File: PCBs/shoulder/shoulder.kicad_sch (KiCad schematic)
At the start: 4 parts

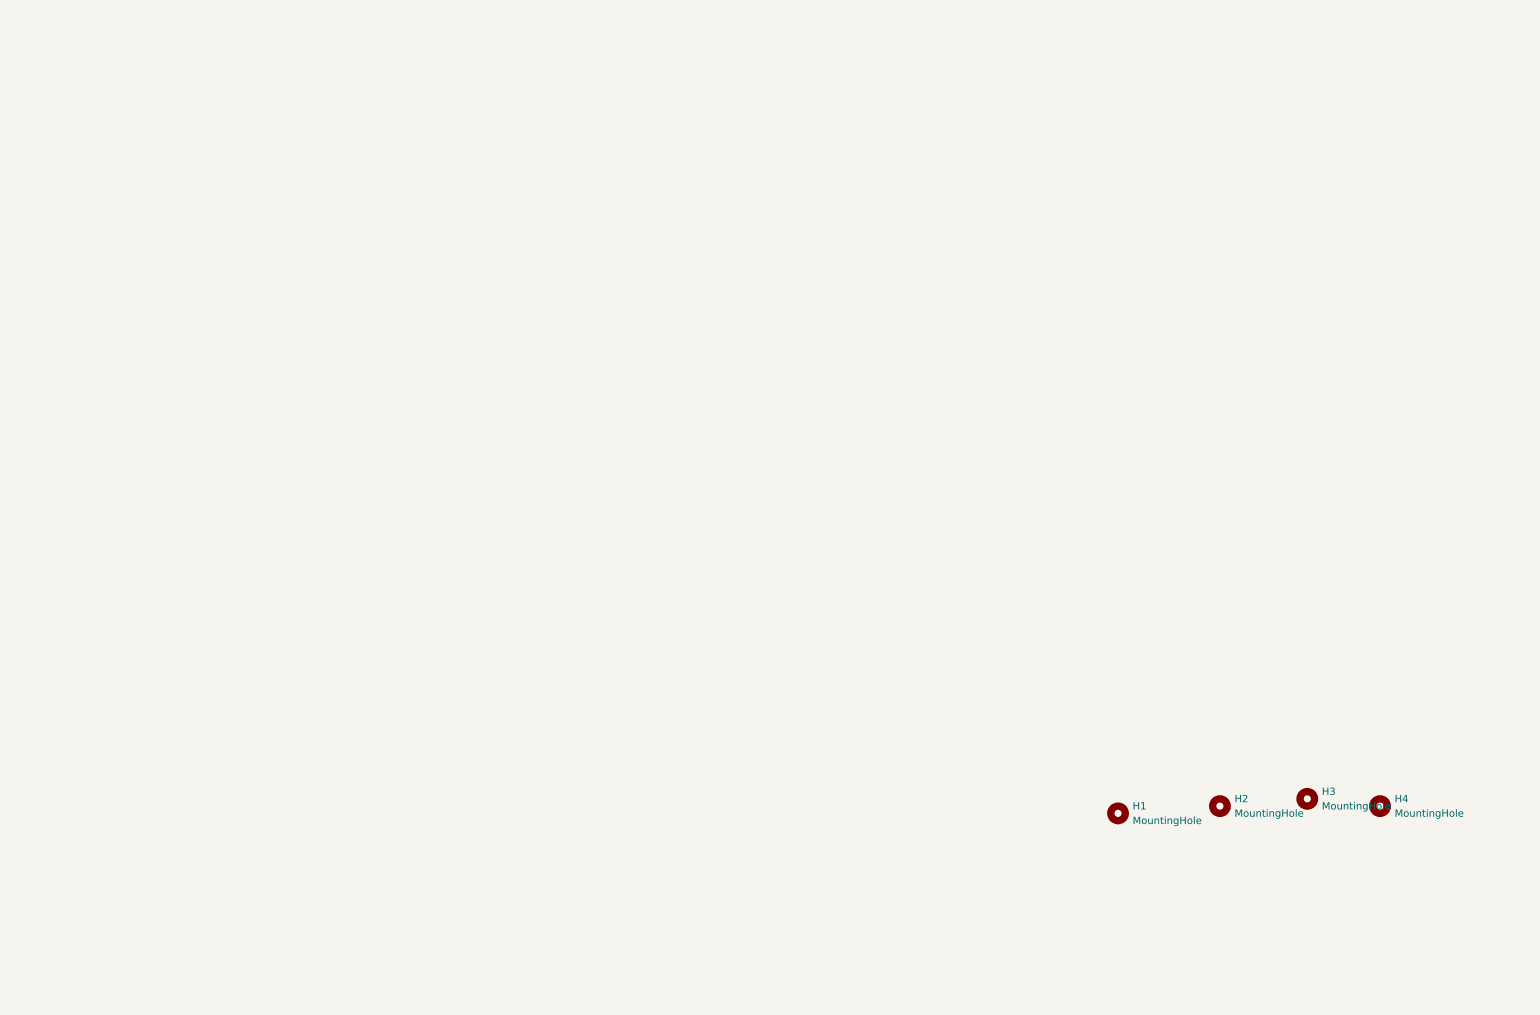
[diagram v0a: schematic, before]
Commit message: Shoulder motor assy almost done. Need to find a library for the 2N551 NPN and redo the circuit. Ensure that the footprint pinout is correct
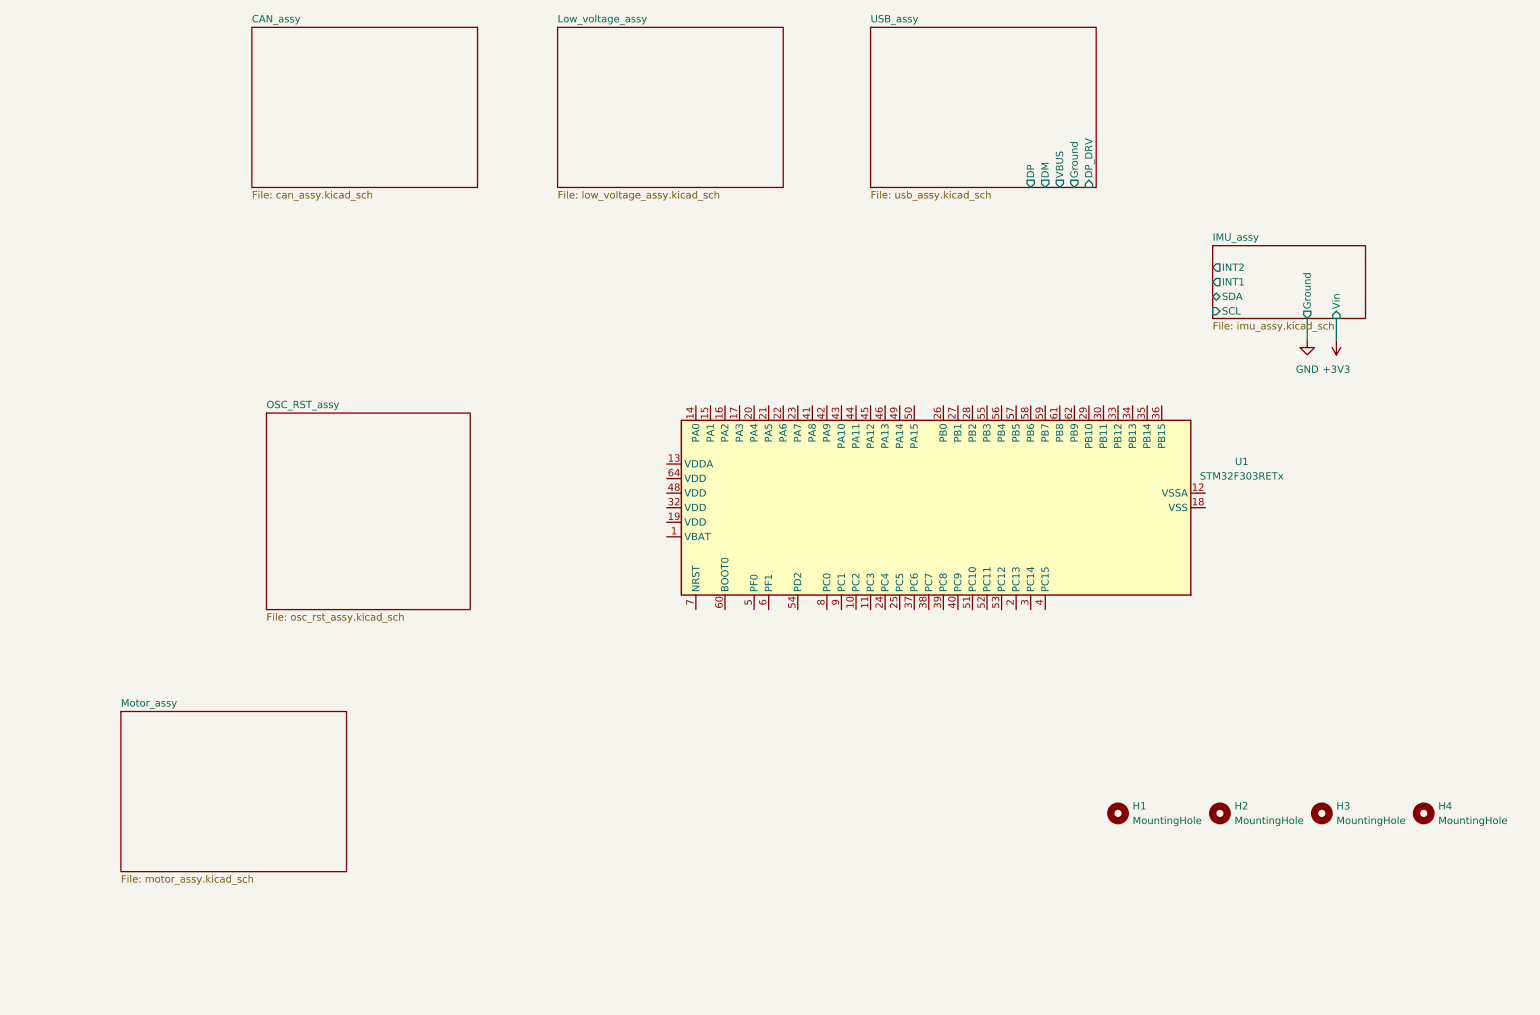
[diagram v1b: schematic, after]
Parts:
- added U1: STM32F303RETx, Package_QFP:LQFP-64_10x10mm_P0.5mm, symbol MCU_ST_STM32F3:STM32F303RETx
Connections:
- new net: U1.18 (VSS), U1.31 (VSS), U1.47 (VSS), U1.63 (VSS)
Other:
- added sheet CAN_assy (can_assy.kicad_sch)
- added sheet IMU_assy (imu_assy.kicad_sch)
- added sheet Low_voltage_assy (low_voltage_assy.kicad_sch)
- added sheet Motor_assy (motor_assy.kicad_sch)
- added sheet OSC_RST_assy (osc_rst_assy.kicad_sch)
- added sheet USB_assy (usb_assy.kicad_sch)
- title: (none) -> Shoulder
- moved on the sheet: H2, H3, H4

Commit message: Torso all but complete, making bogie before checking the last mark
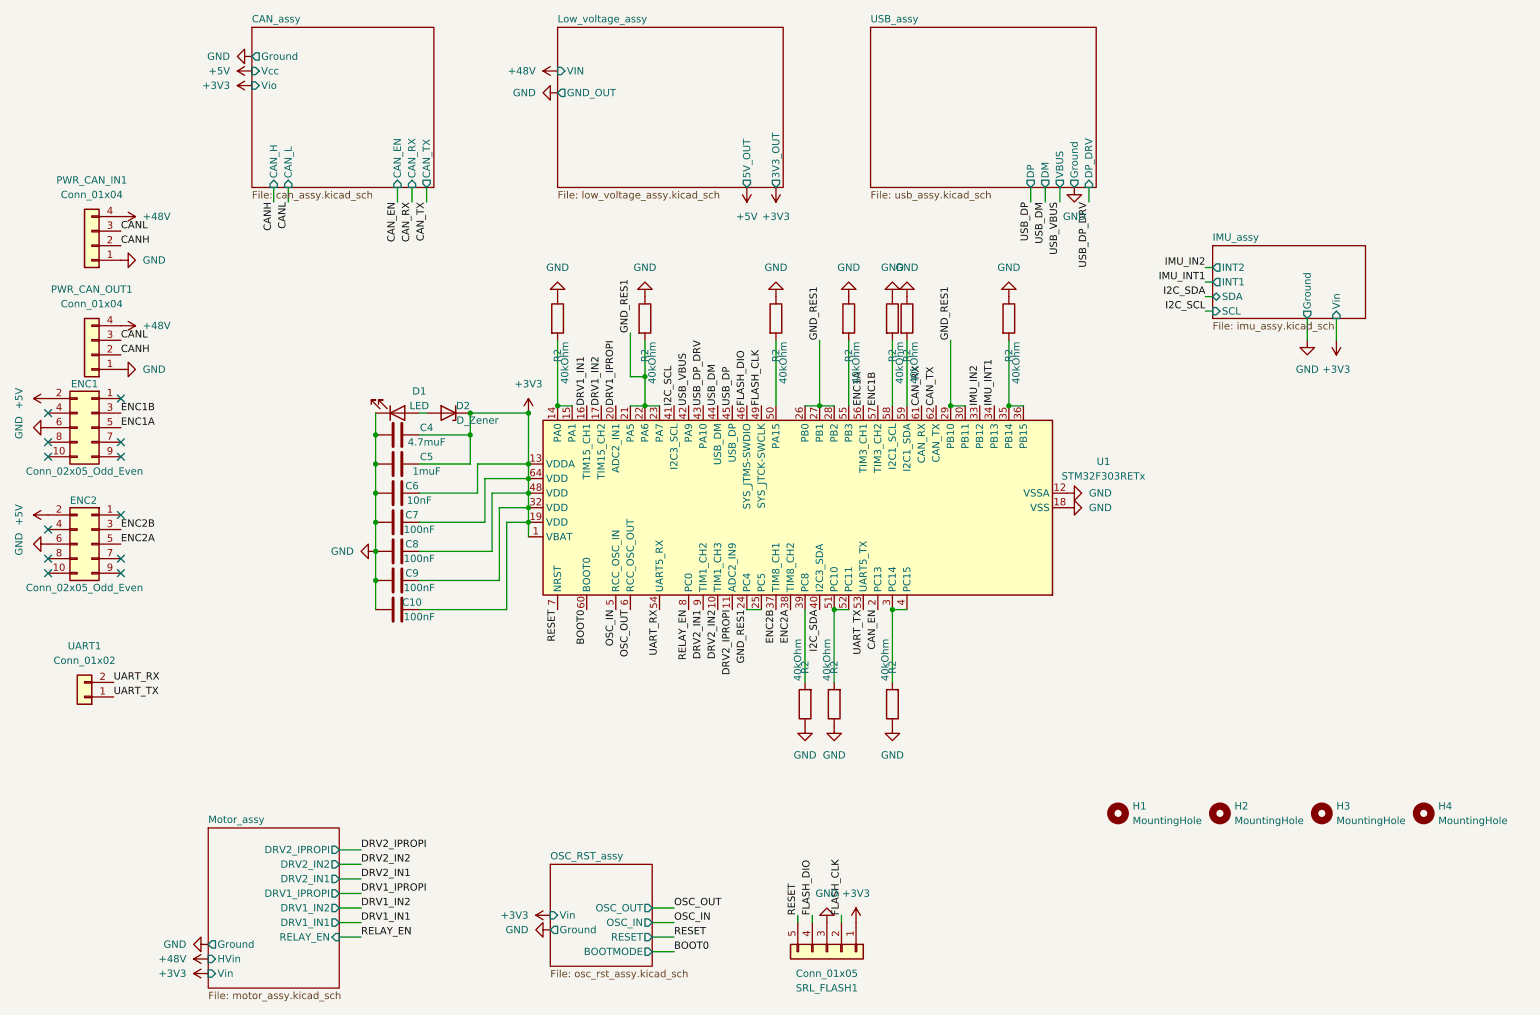
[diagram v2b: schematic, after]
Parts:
- added C10, C7, C8, C9: 100nF, Capacitor_SMD:C_0603_1608Metric, symbol Device:C
- added C4: 4.7muF, Capacitor_SMD:C_0603_1608Metric, symbol Device:C
- added C5: 1muF, Capacitor_SMD:C_0603_1608Metric, symbol Device:C
- added C6: 10nF, Capacitor_SMD:C_0603_1608Metric, symbol Device:C
- added D1: LED, LED_SMD:LED_0603_1608Metric, symbol Device:LED
- added D2: D_Zener, Diode_THT:D_T-1_P5.08mm_Horizontal, symbol Device:D_Zener
- added ENC1, ENC2: Conn_02x05_Odd_Even, Connector_PinHeader_2.54mm:PinHeader_2x05_P2.54mm_Vertical, symbol Connector_Generic:Conn_02x05_Odd_Even
- added PWR_CAN_IN1, PWR_CAN_OUT1: Conn_01x04, TerminalBlock_4Ucon:TerminalBlock_4Ucon_1x04_P3.50mm_Vertical, symbol Connector_Generic:Conn_01x04
- added R2 (x10): 40kOhm, Resistor_SMD:R_0402_1005Metric, symbol Device:R
- added SRL_FLASH1: Conn_01x05, Connector_PinHeader_2.54mm:PinHeader_1x05_P2.54mm_Vertical, symbol Connector_Generic:Conn_01x05
- added UART1: Conn_01x02, Connector_PinHeader_2.54mm:PinHeader_1x02_P2.54mm_Vertical, symbol Connector_Generic:Conn_01x02
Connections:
- net +3V3: now also U1.1 (VBAT), U1.13 (VDDA), U1.19 (VDD), U1.32 (VDD), U1.48 (VDD), U1.64 (VDD), C10.2, C4.1, C5.1, C6.2, C7.2, C8.2, C9.2, D2.1 (K), SRL_FLASH1.1 (Pin_1)
- net GND: now also U1.12 (VSSA), U1.18 (VSS), U1.31 (VSS), U1.47 (VSS), U1.63 (VSS), C10.1, C4.2, C5.2, C6.1, C7.1, C8.1, C9.1, D1.1 (K), ENC1.6 (Pin_6), ENC2.6 (Pin_6), PWR_CAN_IN1.1 (GND), PWR_CAN_OUT1.1 (GND), R2.1, R2.1, R2.1, R2.1, R2.1, R2.1, R2.1, R2.1, R2.1, R2.1, SRL_FLASH1.3 (Pin_3)
- net DRV2_IN2: now reaches U1.10 (PC2)
- net DRV2_IPROPI: now reaches U1.11 (PC3)
- net at U1.14 (PA0): now also U1.15 (PA1), R2.2
- net DRV1_IN1: now reaches U1.16 (PA2)
- net DRV1_IN2: now reaches U1.17 (PA3)
- net CAN_EN: now reaches U1.2 (PC13)
- net DRV1_IPROPI: now reaches U1.20 (PA4)
- net GND_RES1: now reaches U1.21 (PA5)
- net GND_RES1: now also U1.22 (PA6), U1.23 (PA7), U1.24 (PC4), U1.25 (PC5), U1.26 (PB0), U1.27 (PB1), U1.28 (PB2), U1.29 (PB10), U1.30 (PB11), R2.2
- net at U1.3 (PC14): now also U1.4 (PC15), R2.2
- net IMU_IN2: now reaches U1.33 (PB12)
- net IMU_INT1: now reaches U1.34 (PB13)
- net at U1.35 (PB14): now also U1.36 (PB15), R2.2
- net ENC2B: now reaches U1.37 (PC6)
- net ENC2B: now also ENC2.3 (Pin_3)
- net ENC2A: now reaches U1.38 (PC7)
- net ENC2A: now also ENC2.5 (Pin_5)
- net at U1.39 (PC8): now also R2.2
- net I2C_SDA: now reaches U1.40 (PC9)
- net I2C_SCL: now reaches U1.41 (PA8)
- net USB_VBUS: now reaches U1.42 (PA9)
- net USB_DP_DRV: now reaches U1.43 (PA10)
- net USB_DM: now reaches U1.44 (PA11)
- net USB_DP: now reaches U1.45 (PA12)
- net FLASH_DIO: now reaches U1.46 (PA13)
- net FLASH_DIO: now also SRL_FLASH1.4 (Pin_4)
- net FLASH_CLK: now reaches U1.49 (PA14)
- net FLASH_CLK: now also SRL_FLASH1.2 (Pin_2)
- net OSC_IN: now reaches U1.5 (PF0)
- net at U1.50 (PA15): now also R2.2
- net at U1.51 (PC10): now also U1.52 (PC11), R2.2
- net UART_TX: now reaches U1.53 (PC12)
- net UART_TX: now also UART1.1 (Pin_1)
- net UART_RX: now reaches U1.54 (PD2)
- net UART_RX: now also UART1.2 (Pin_2)
- net at U1.55 (PB3): now also R2.2
- net ENC1A: now reaches U1.56 (PB4)
- net ENC1A: now also ENC1.5 (Pin_5)
- net ENC1B: now reaches U1.57 (PB5)
- net ENC1B: now also ENC1.3 (Pin_3)
- net at U1.58 (PB6): now also R2.2
- net at U1.59 (PB7): now also R2.2
- net OSC_OUT: now reaches U1.6 (PF1)
- net BOOT0: now reaches U1.60 (BOOT0)
- net CAN_RX: now reaches U1.61 (PB8)
- net CAN_TX: now reaches U1.62 (PB9)
- net RESET: now reaches U1.7 (NRST)
- net RESET: now also SRL_FLASH1.5 (Pin_5)
- net RELAY_EN: now reaches U1.8 (PC0)
- net DRV2_IN1: now reaches U1.9 (PC1)
- new net: D1.2 (A), D2.2 (A)
- new net +48V: PWR_CAN_IN1.4 (48V), PWR_CAN_OUT1.4 (48V)
- new net +5V: ENC1.2 (Pin_2), ENC2.2 (Pin_2)
- new net CANH: PWR_CAN_IN1.2 (CANH), PWR_CAN_OUT1.2 (CANH)
- new net CANL: PWR_CAN_IN1.3 (CANL), PWR_CAN_OUT1.3 (CANL)
- no-connect marks 0 -> 12
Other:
- sheet CAN_assy ports: added CAN_EN, CAN_H, CAN_L, CAN_RX, CAN_TX, Ground, Vcc, Vio; removed none
- sheet Low_voltage_assy ports: added 3V3_OUT, 5V_OUT, GND_OUT, VIN; removed none
- sheet Motor_assy ports: added DRV1_IN1, DRV1_IN2, DRV1_IPROPI, DRV2_IN1, DRV2_IN2, DRV2_IPROPI, Ground, HVin, RELAY_EN, Vin; removed none
- sheet OSC_RST_assy ports: added BOOTMODE, Ground, OSC_IN, OSC_OUT, RESET, Vin; removed none
- moved on the sheet: U1

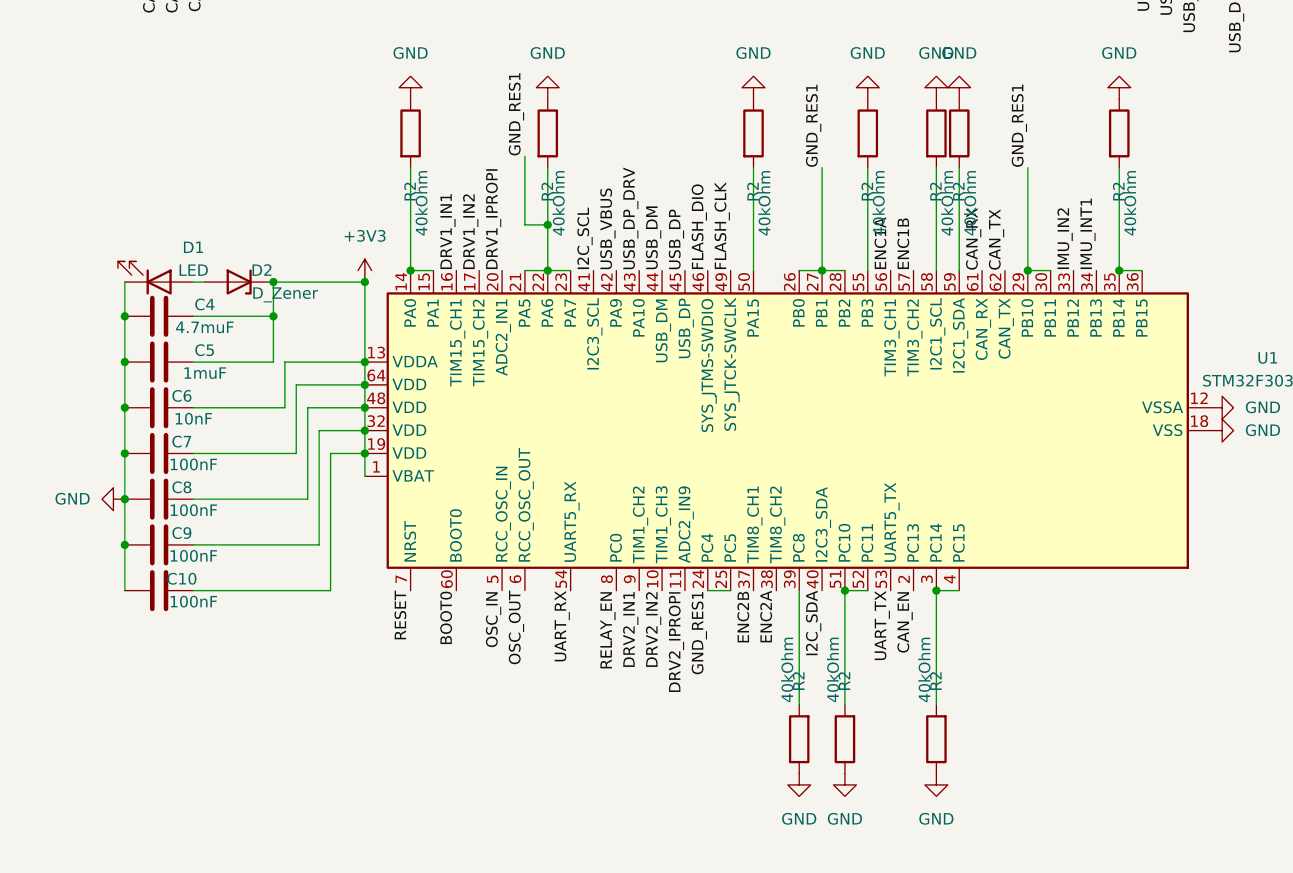
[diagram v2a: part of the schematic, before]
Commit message: merged changes from timertests, mostly documentation and such. Did not add tim6 config
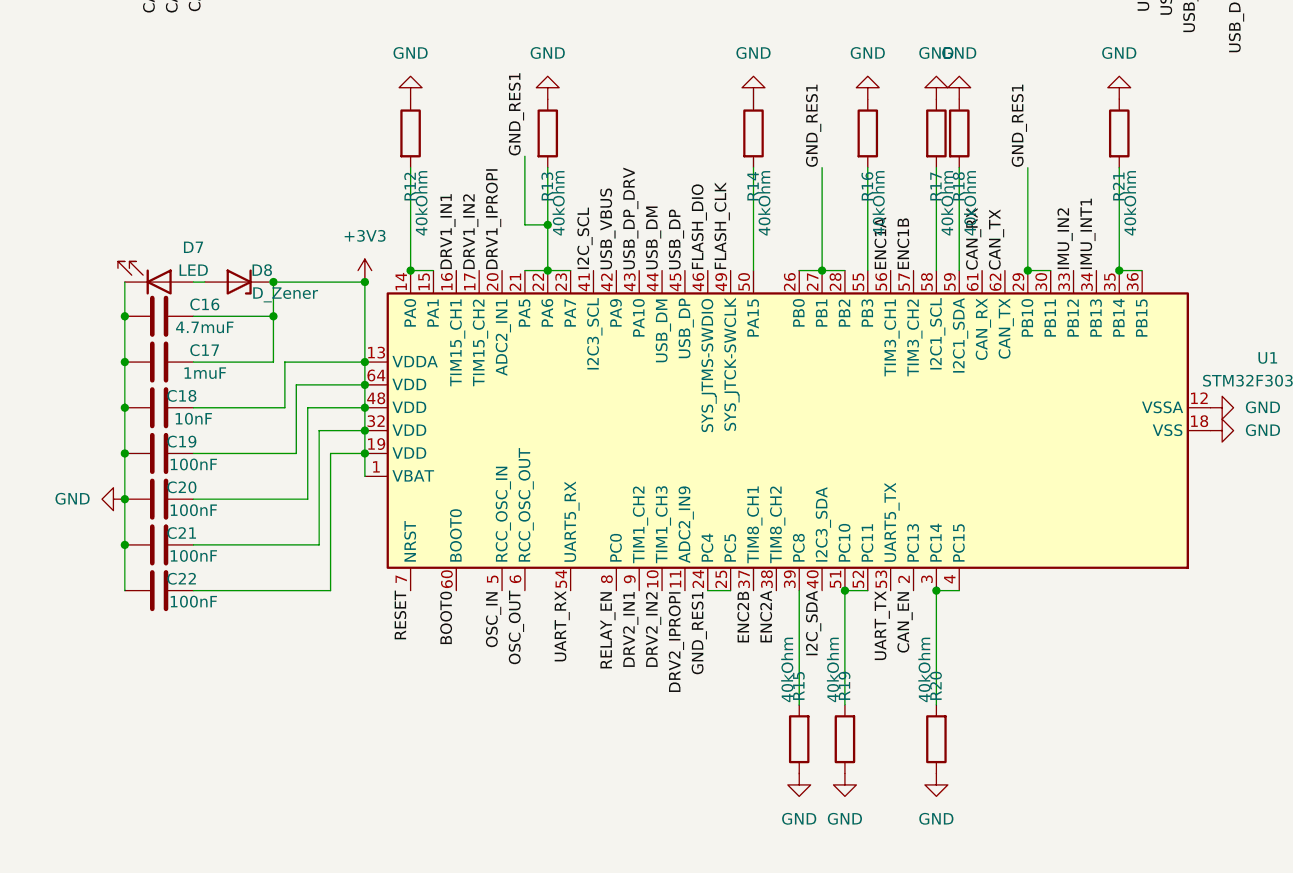
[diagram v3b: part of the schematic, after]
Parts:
- renumbered C4 to C16, C5 to C17, C6 to C18, C7 to C19, C8 to C20, C9 to C21, C10 to C22, D1 to D7, D2 to D8, R2 to R12, R2 to R13, R2 to R14, R2 to R15, R2 to R16, R2 to R17, R2 to R18, R2 to R19, R2 to R20, R2 to R21
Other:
- title: Shoulder -> Shoulder PCB
